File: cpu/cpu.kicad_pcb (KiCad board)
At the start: 4 copper layers, 84 x 40 mm, 40 parts, among them J2 Conn_01x08, Q3 2N7002, U1 ICE40HX1K-VQ100_RV4028, U2 W25Q80DVSS, U3 AP2112K-1.2

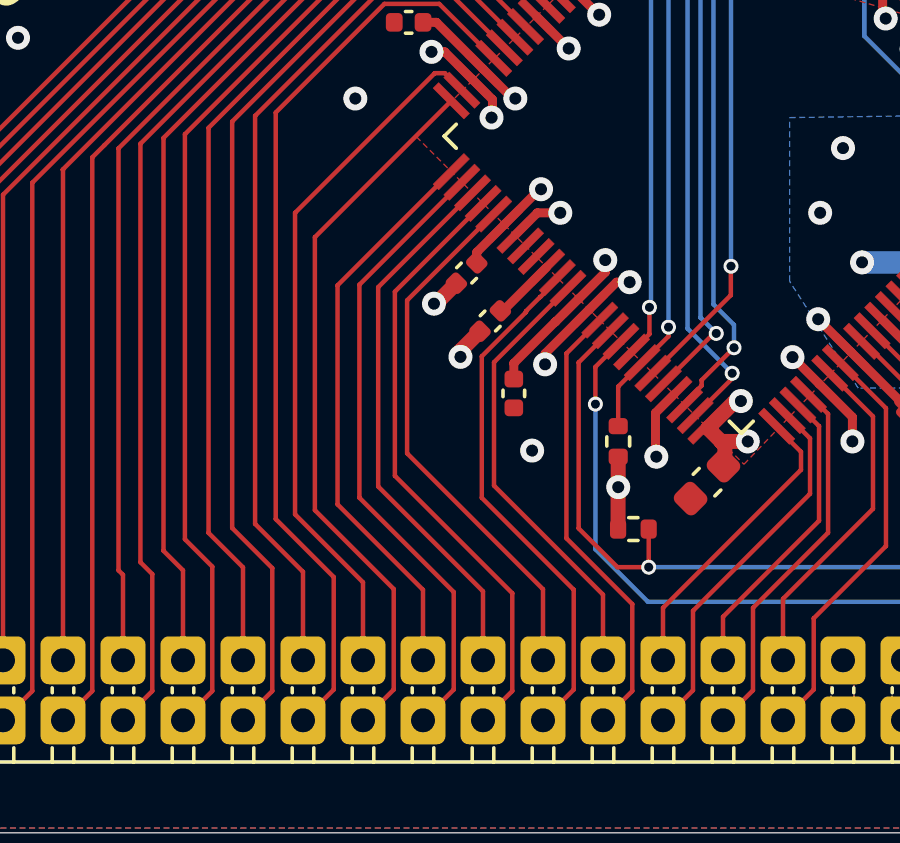
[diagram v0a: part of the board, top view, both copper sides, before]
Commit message: Review before first PCB order
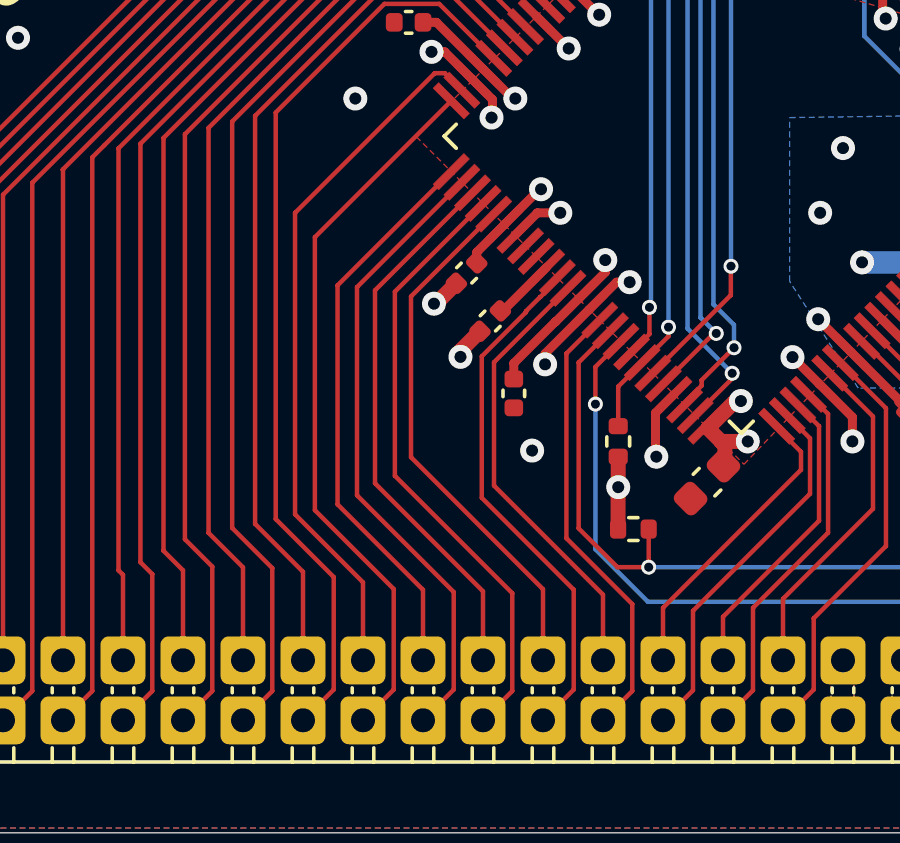
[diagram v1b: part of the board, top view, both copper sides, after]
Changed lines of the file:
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@@
 			)
 		)
+		(property "JLC" "C5383116"
+			(at 0 0 270)
+			(unlocked yes)
+			(layer "F.Fab")
+			(hide yes)
+			(effects
+				(font
+					(size 1 1)
+					(thickness 0.15)
+				)
+			)
+		)
 		(property ki_fp_filters "Connector*:*_1x??_*")
 		(sheetname "/")
 		(sheetfile "cpu.kicad_sch")
-		(attr through_hole dnp)
+		(attr through_hole)
 		(fp_line
 			(start -1.77 19.55)
@@
 	)
 	(segment
-		(start 115.356932 100.624932)
-		(end 115.345652 100.624932)
+		(start 117 113.1298)
+		(end 117 115.5)
 		(width 0.15)
 		(layer "F.Cu")
@@
 	)
 	(segment
-		(start 117 115.5)
-		(end 117 113.1298)
+		(start 115.345652 100.624932)
+		(end 112.6 103.370584)
 		(width 0.15)
 		(layer "F.Cu")
@@
 	)
 	(segment
-		(start 117 113.1298)
-		(end 112.4702 108.6)
+		(start 112.6 103.370584)
+		(end 112.6 108.7298)
 		(width 0.15)
 		(layer "F.Cu")
@@
 	)
 	(segment
-		(start 115.345652 100.624932)
-		(end 112.4702 103.500384)
+		(start 115.356932 100.624932)
+		(end 115.345652 100.624932)
 		(width 0.15)
 		(layer "F.Cu")
@@
 	)
 	(segment
-		(start 112.4702 103.500384)
-		(end 112.4702 108.6)
+		(start 112.6 108.7298)
+		(end 117 113.1298)
 		(width 0.15)
 		(layer "F.Cu")
@@
 	)
 	(segment
-		(start 110.880272 110.080272)
-		(end 110.880272 102.980272)
+		(start 114.024 113.224)
+		(end 110.8 110)
 		(width 0.15)
 		(layer "F.Cu")
@@
 	)
 	(segment
-		(start 113 117.5)
-		(end 114.024 116.476)
+		(start 110.8 110)
+		(end 110.8 103.060544)
 		(width 0.15)
 		(layer "F.Cu")
@@
 	)
 	(segment
-		(start 114.024 113.224)
-		(end 110.880272 110.080272)
+		(start 110.8 103.060544)
+		(end 114.296272 99.564272)
 		(width 0.15)
 		(layer "F.Cu")
@@
 	)
 	(segment
-		(start 114.024 116.476)
-		(end 114.024 113.224)
+		(start 113 117.5)
+		(end 114.024 116.476)
 		(width 0.15)
 		(layer "F.Cu")
@@
 	)
 	(segment
-		(start 110.880272 102.980272)
-		(end 114.296272 99.564272)
+		(start 114.024 116.476)
+		(end 114.024 113.224)
 		(width 0.15)
 		(layer "F.Cu")
@@
 	)
 	(segment
-		(start 111.506 109.706)
-		(end 111.506 103.06165)
+		(start 111.4 109.6)
+		(end 111.4 103.16765)
 		(width 0.15)
 		(layer "F.Cu")
@@
 	)
 	(segment
-		(start 111.506 103.06165)
+		(start 111.4 103.16765)
 		(end 114.649825 99.917825)
 		(width 0.15)
@@
 	(segment
 		(start 115 113.2)
-		(end 111.506 109.706)
+		(end 111.4 109.6)
 		(width 0.15)
 		(layer "F.Cu")

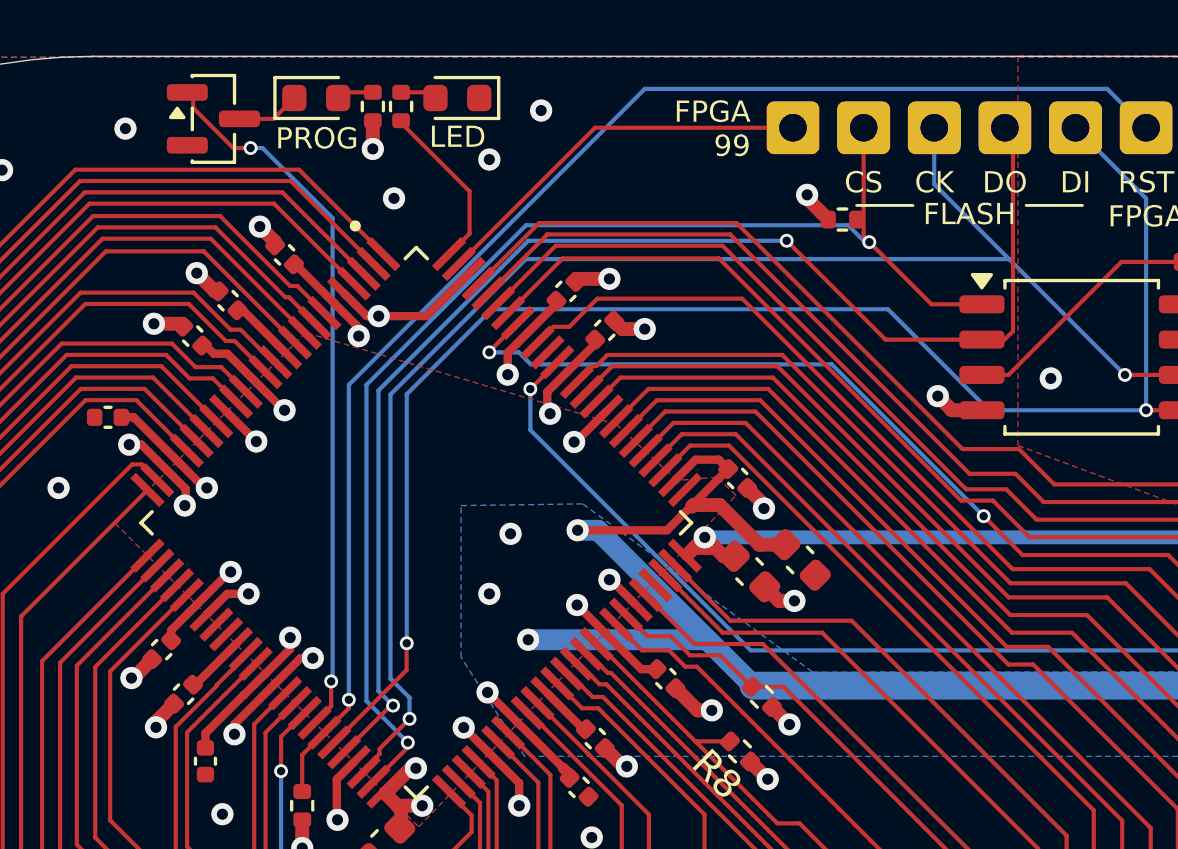
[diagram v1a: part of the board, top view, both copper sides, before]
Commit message: Updates from ICE40 checklist
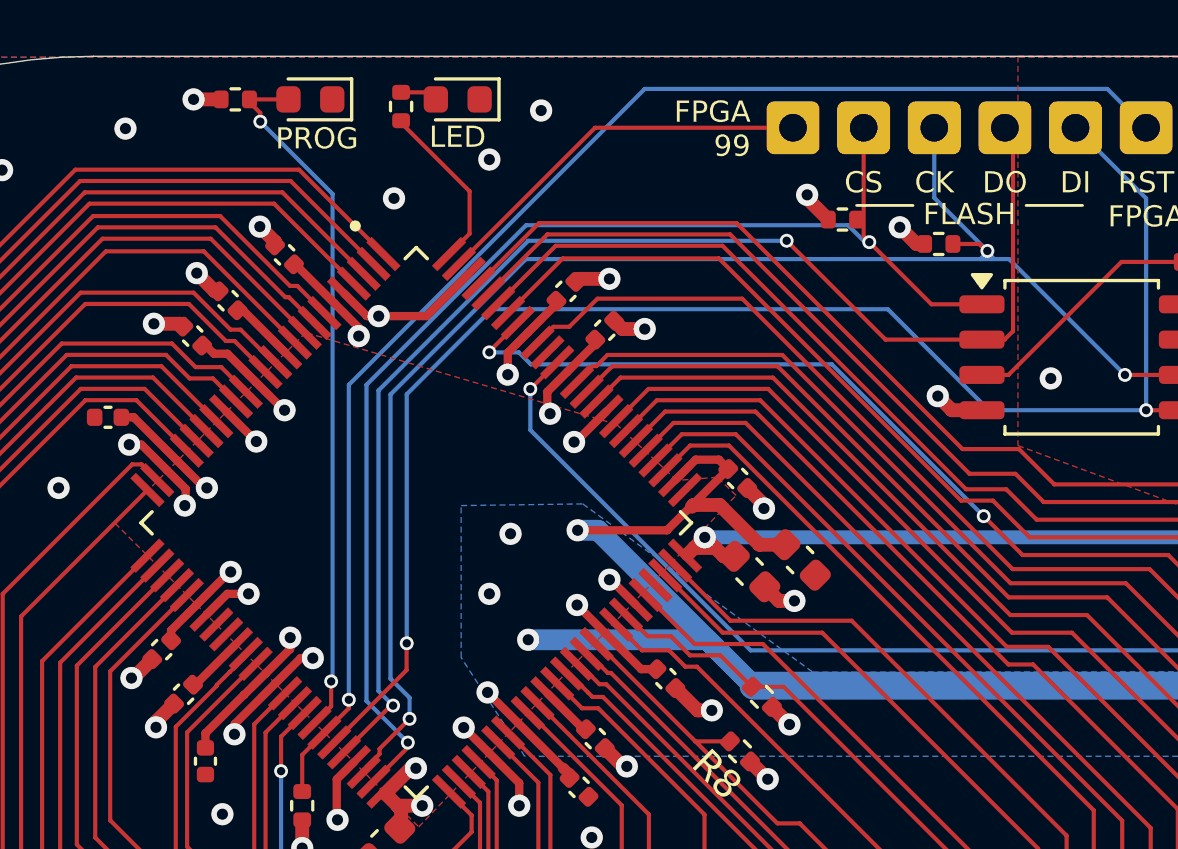
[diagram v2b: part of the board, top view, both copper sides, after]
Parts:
- removed Q3: 2N7002, Package_TO_SOT_SMD:SOT-23
- added R9: 10k, Resistor_SMD:R_0402_1005Metric, F.Cu at (142.4, 88.0)
- R1, R2: value 1k -> 10k
- R3, R7: value 1k -> 2.2k
- moved R3 4.95 mm to (117.1, 82.8), turned to 0 degrees
- moved D3 0.22 mm to (119.8, 82.8), turned to 180 degrees
- moved D2 0.05 mm to (125.1, 82.8)
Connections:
- D3 pad 1: Net-(D3-K) -> GND
- D3 pad 2: Net-(D3-A) -> CDONE
- R3 pad 2: Net-(D3-A) -> CDONE
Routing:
- net SPI_CLK: track 52.6 -> 55.0 mm, vias 2 -> 3
- net Net-(D3-K): track 2.29 -> 0.00 mm
- net Net-(D3-A): track 1.27 -> 0.00 mm
- net +3V3: track 50.1 -> 51.1 mm, vias 20 -> 21
